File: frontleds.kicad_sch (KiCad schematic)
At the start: 5 parts, among them J19 Conn_01x02, J20 Conn_01x02, U18 DMG2305UX-7

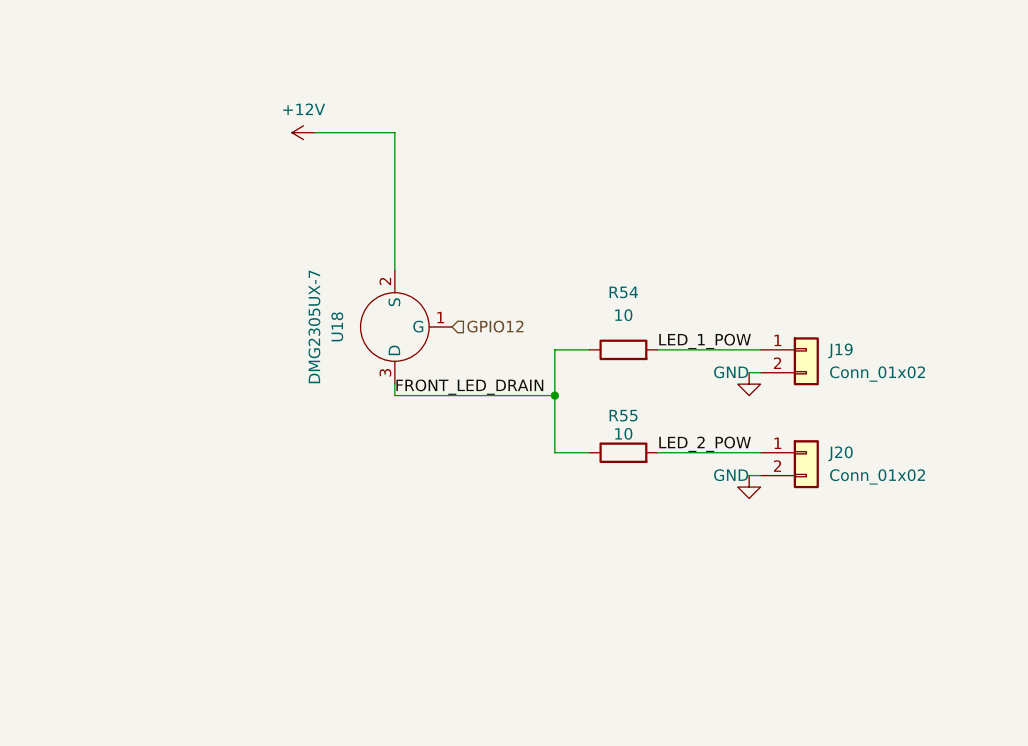
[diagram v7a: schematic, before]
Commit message: added edge connector sockets to main pcb and changed led power source to 3.3v
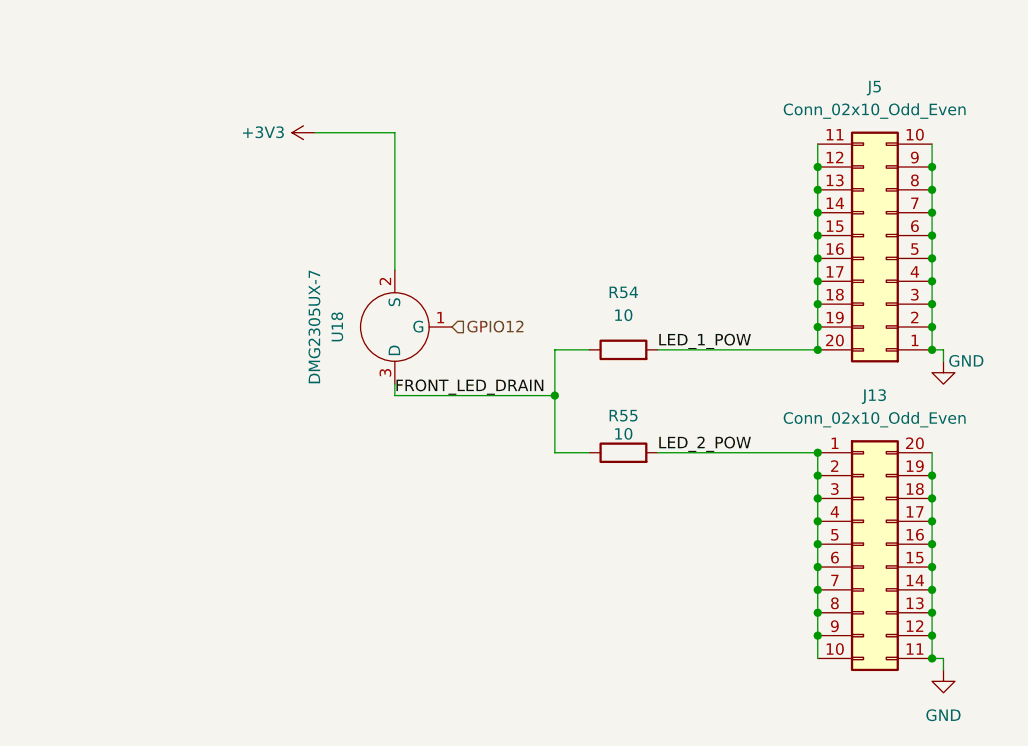
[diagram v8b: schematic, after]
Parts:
- removed J19, J20: Conn_01x02, Connector_JST:JST_PH_B2B-PH-K_1x02_P2.00mm_Vertical, symbol Connector_Generic:Conn_01x02
- added J13, J5: Conn_02x10_Odd_Even, Connector_Samtec_HSEC8:Samtec_HSEC8-110-01-X-DV-A_2x10_P0.8mm_Socket_AlignmentPins, symbol Connector_Generic:Conn_02x10_Counter_Clockwise
- R54, R55: footprint Resistor_SMD:R_0402_1005Metric -> Resistor_SMD:R_2512_6332Metric
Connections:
- net GND: now also J13.11 (Pin_11), J13.12 (Pin_12), J13.13 (Pin_13), J13.14 (Pin_14), J13.15 (Pin_15), J13.16 (Pin_16), J13.17 (Pin_17), J13.18 (Pin_18), J13.19 (Pin_19), J13.20 (Pin_20), J5.1 (Pin_1), J5.10 (Pin_10), J5.2 (Pin_2), J5.3 (Pin_3), J5.4 (Pin_4), J5.5 (Pin_5), J5.6 (Pin_6), J5.7 (Pin_7), J5.8 (Pin_8), J5.9 (Pin_9)
- net LED_1_POW: now also J5.11 (Pin_11), J5.12 (Pin_12), J5.13 (Pin_13), J5.14 (Pin_14), J5.15 (Pin_15), J5.16 (Pin_16), J5.17 (Pin_17), J5.18 (Pin_18), J5.19 (Pin_19), J5.20 (Pin_20)
- net LED_2_POW: now also J13.1 (Pin_1), J13.10 (Pin_10), J13.2 (Pin_2), J13.3 (Pin_3), J13.4 (Pin_4), J13.5 (Pin_5), J13.6 (Pin_6), J13.7 (Pin_7), J13.8 (Pin_8), J13.9 (Pin_9)
- net +12V renamed +3V3
